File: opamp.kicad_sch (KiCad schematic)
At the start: 16 parts, among them J62 Conn_01x05, J63 Conn_01x03, J64 Conn_01x03, J65 Conn_01x03, J66 Conn_01x03, J67 Conn_01x05, Q10 SS8050, Q11 SS8050, Q12 SS8050, Q13 SS8050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

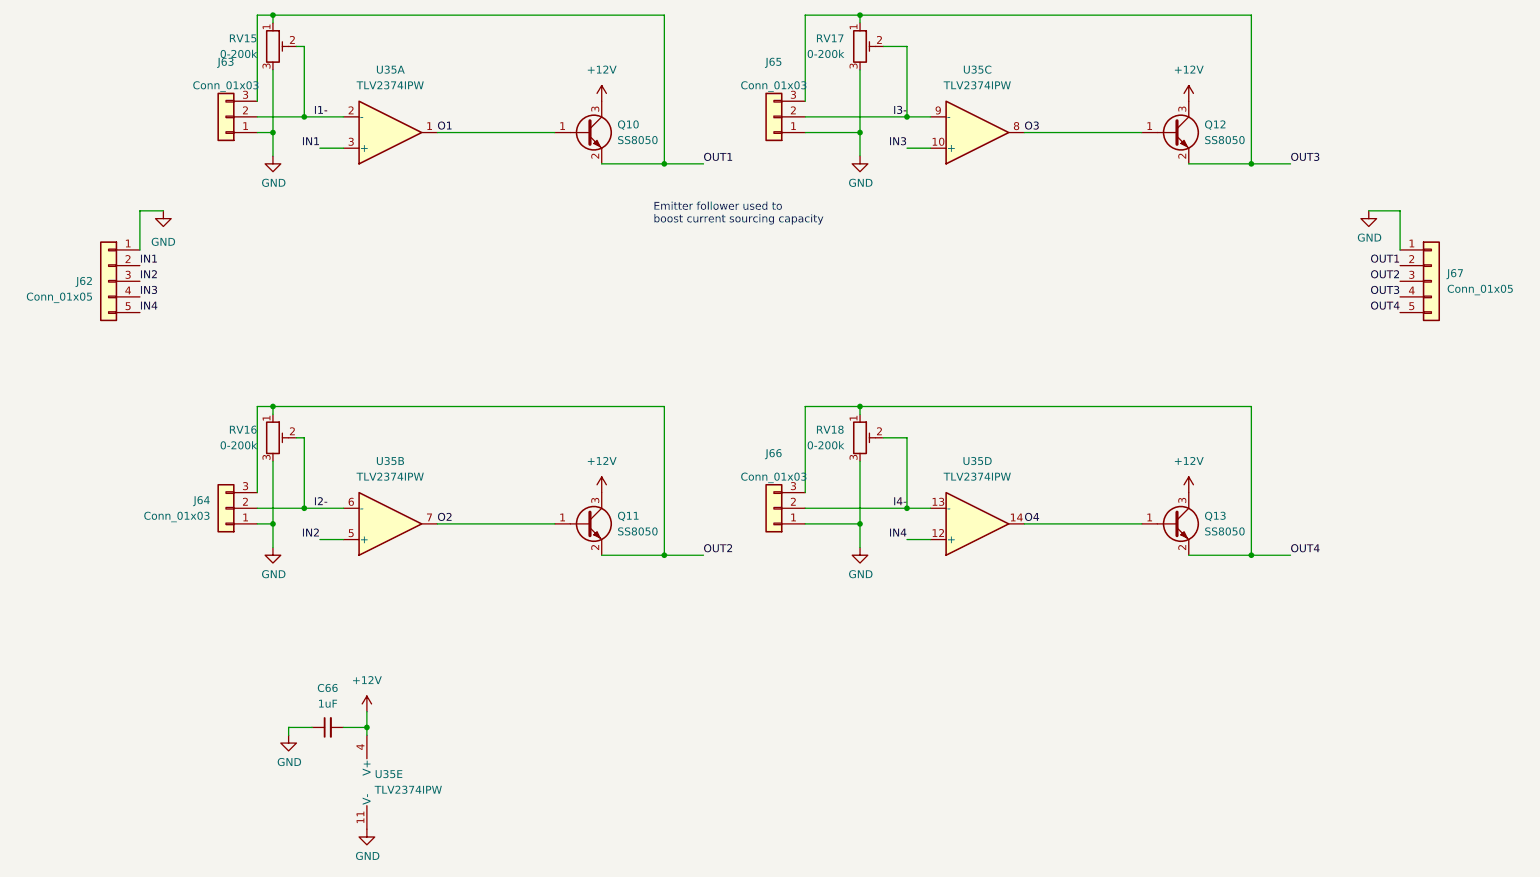
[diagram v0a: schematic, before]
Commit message: Update the design to a stackable one
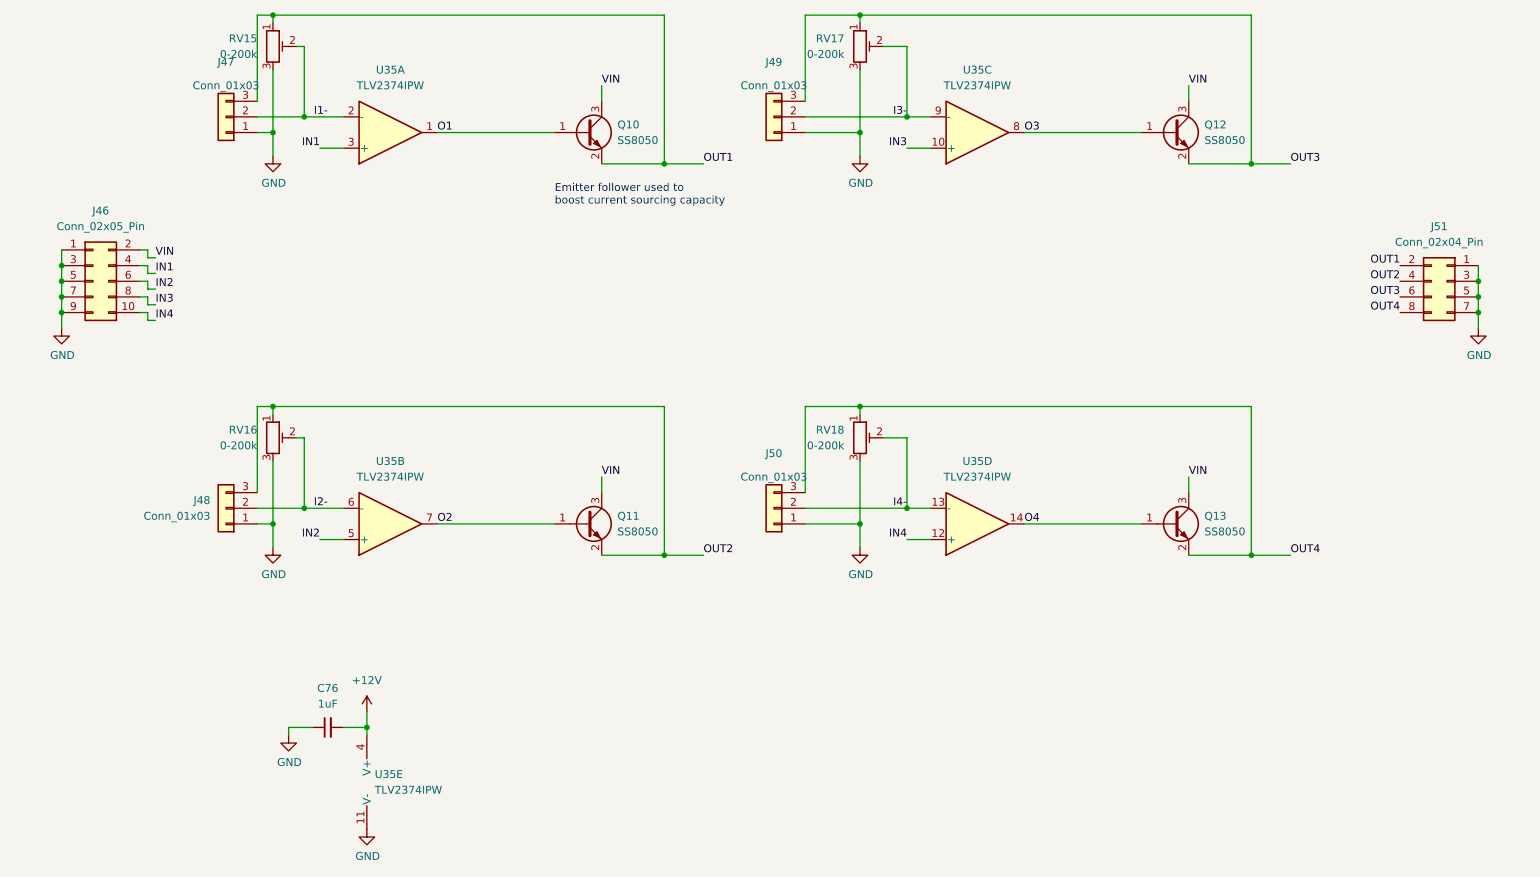
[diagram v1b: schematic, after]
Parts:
- J46: renamed from J62; value Conn_01x05 -> Conn_02x05_Pin; footprint HL_Connector_Pad_2.54mm:Pad_1x05_P2.54_1.7x1.7_Rect-Oct -> HL_Connector_Pad_2.54mm:Pad_2x05_P2.54_1.7x1.7_Rect-1Rnd-4Oct; symbol Connector_Generic:Conn_01x05 -> Connector_Generic:Conn_02x05_Odd_Even; JLCPCB_CORRECTION 0;5.08;270 -> 1.27;-5.08;270; LCSC C492404 -> C5383106
- J51: renamed from J67; value Conn_01x05 -> Conn_02x04_Pin; footprint HL_Connector_Pad_2.54mm:Pad_1x05_P2.54_1.7x1.7_Rect-Oct -> HL_Connector_Pad_2.54mm:Pad_2x04_P2.54_1.7x1.7_Rect-Oct; symbol Connector_Generic:Conn_01x05 -> Connector_Generic:Conn_02x04_Odd_Even; JLCPCB_CORRECTION 0;5.08;270 -> 1.27;-3.81;270; LCSC C492404 -> C5383105
- renumbered C66 to C76, J63 to J47, J64 to J48, J65 to J49, J66 to J50
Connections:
- net +12V: no longer Q10.3 (C), Q11.3 (C), Q12.3 (C), Q13.3 (C)
- net GND: now also J46.3 (Pin_3), J46.5 (Pin_5), J46.7 (Pin_7), J46.9 (Pin_9), J51.3 (Pin_3), J51.5 (Pin_5), J51.7 (Pin_7)
- net IN1: now also J46.4 (Pin_4); no longer J46.2 (Pin_2)
- net IN2: now also J46.6 (Pin_6); no longer J46.3 (Pin_3)
- net IN3: now also J46.8 (Pin_8); no longer J46.4 (Pin_4)
- net IN4: now also J46.10 (Pin_10); no longer J46.5 (Pin_5)
- net OUT2: now also J51.4 (Pin_4); no longer J51.3 (Pin_3)
- net OUT3: now also J51.6 (Pin_6); no longer J51.4 (Pin_4)
- net OUT4: now also J51.8 (Pin_8); no longer J51.5 (Pin_5)
- new net VIN: J46.2 (Pin_2), Q10.3 (C), Q11.3 (C), Q12.3 (C), Q13.3 (C)
